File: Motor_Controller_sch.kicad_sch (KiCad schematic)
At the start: 34 parts, among them J10 1190304, J15 1190304, J17 Barrel_Jack, J2 GND, J3 RX, J4 TX, J5 RESET, J6 1098168, J9 1098168, U5 MCP23017_SP, U6 ATmega328-P, U7 L7805, U8 ULN2003

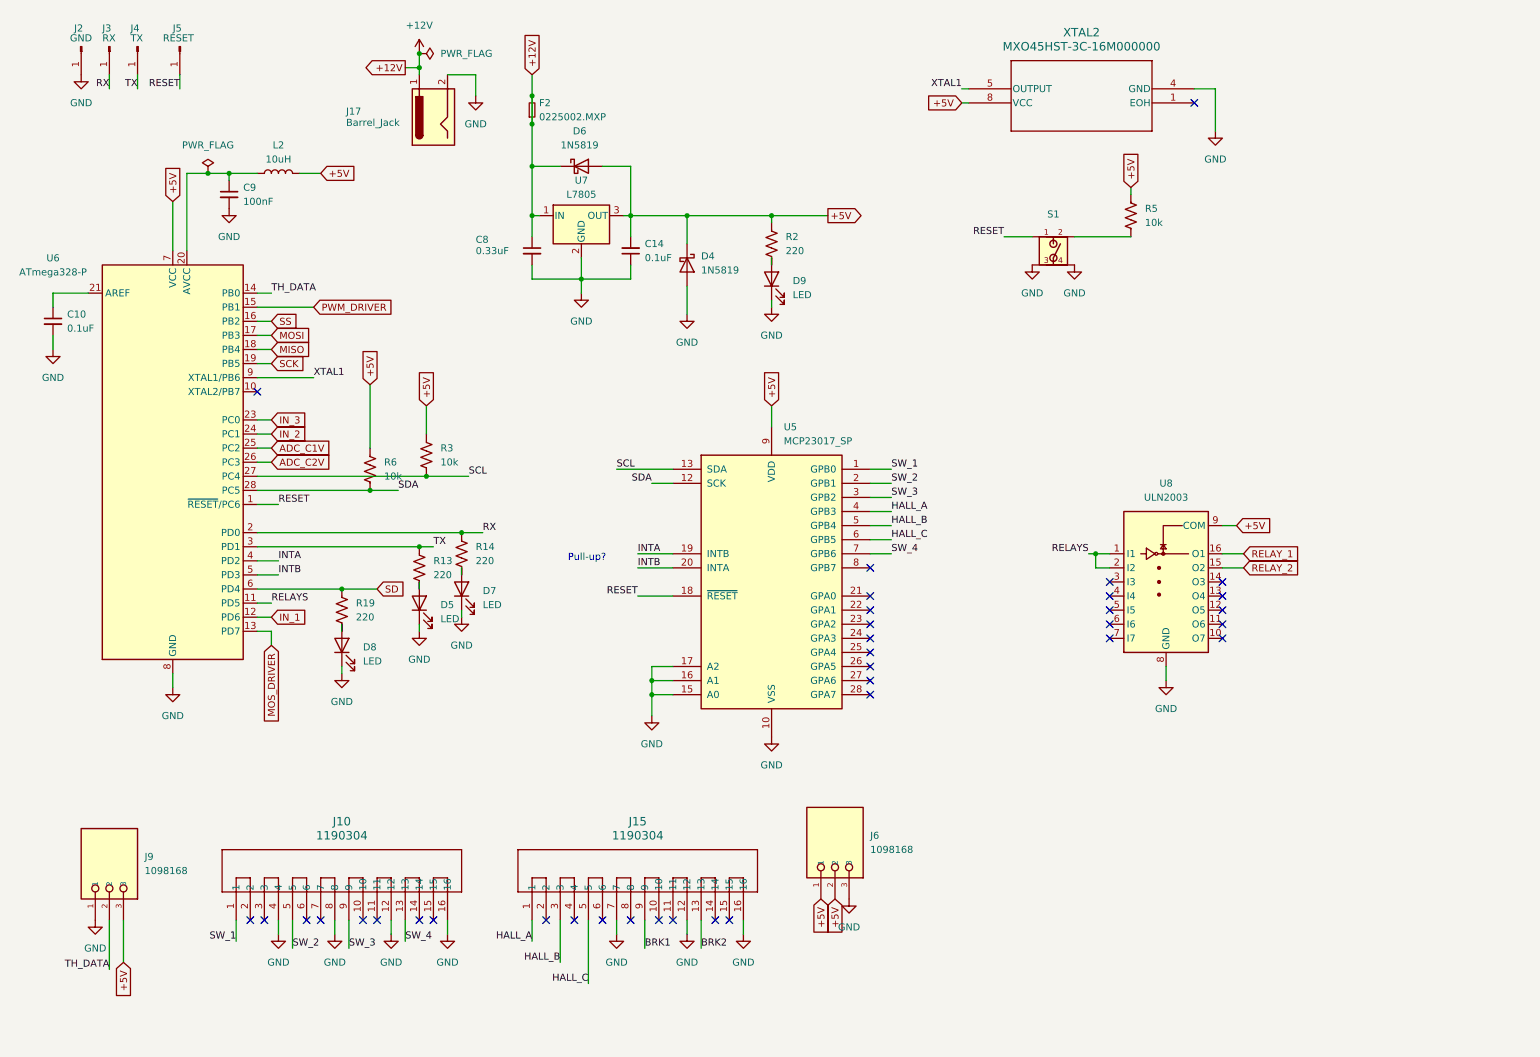
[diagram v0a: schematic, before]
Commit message: Made progress on the PCB, and adressed small issues regarding the schematic
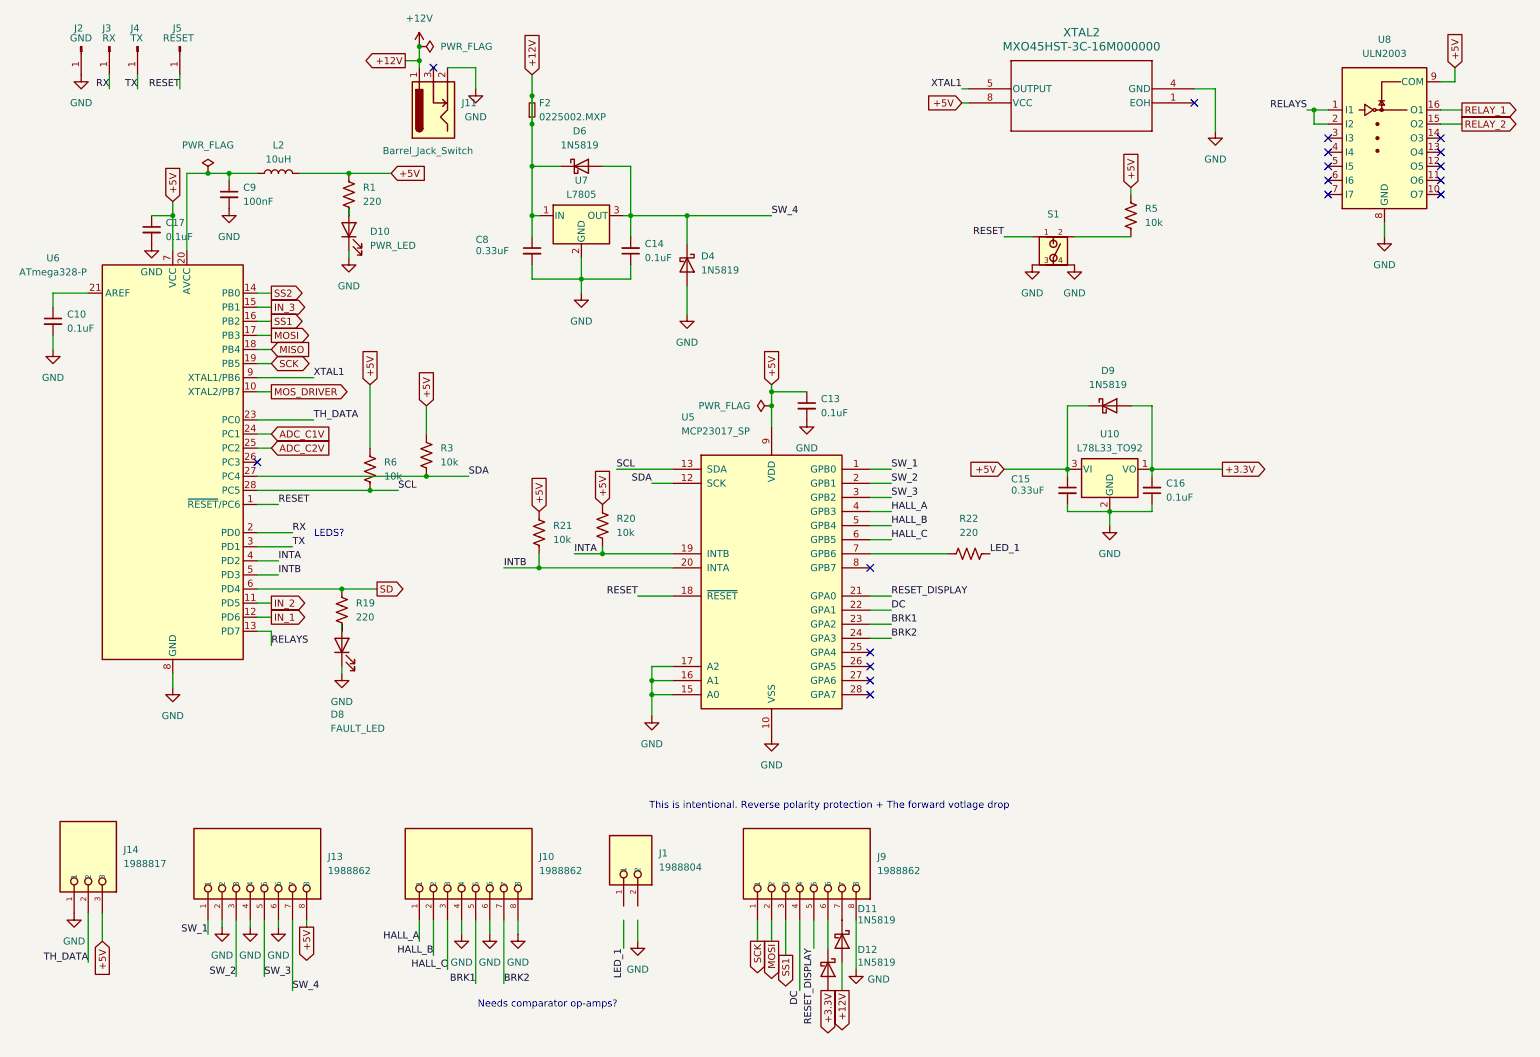
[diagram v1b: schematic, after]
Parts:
- removed D5, D7, D9: LED, symbol Device:LED
- removed J10, J15: 1190304, CONN16_1190304_PXC, symbol Terminal_1190304:1190304
- removed J17: Barrel_Jack, symbol Connector:Barrel_Jack
- removed J6, J9: 1098168, 1098168:PHOENIX_1098168, symbol Terminal_1098168:1098168
- removed R13, R14, R2: 220, symbol Device:R_US
- added C13, C16, C17: 0.1uF, Ceramic_Cap_5.08mm_Spacing:Ceramic_Cap_5.08mm_Spacing, symbol Device:C_Small
- added C15: 0.33uF, Ceramic_Cap_5.08mm_Spacing:Ceramic_Cap_5.08mm_Spacing, symbol Device:C_Small
- added D10: PWR_LED, LED_THT:LED_D5.0mm, symbol Device:LED
- added D11, D12, D9: 1N5819, Diode_THT:D_DO-41_SOD81_P10.16mm_Horizontal, symbol Diode:1N5819
- added J1: 1988804, Terminal_1988804:CONN_1988804, symbol 1988804:1988804
- added J10, J13, J9: 1988862, Terminal_1988862:PHOENIX_1988862, symbol 1988862:1988862
- added J11: Barrel_Jack_Switch, Barrel_Jack_PJ_002AH:PJ-002AH_CUD, symbol Connector:Barrel_Jack_Switch
- added J14: 1988817, Terminal_1988817:PHOENIX_1988817, symbol 1988817:1988817
- added R1, R22: 220, Resistor_THT:R_Axial_DIN0207_L6.3mm_D2.5mm_P10.16mm_Horizontal, symbol Device:R_US
- added R20, R21: 10k, Resistor_THT:R_Axial_DIN0207_L6.3mm_D2.5mm_P10.16mm_Horizontal, symbol Device:R_US
- added U10: L78L33_TO92, Package_TO_SOT_THT:TO-92_Inline, symbol Regulator_Linear:L78L33_TO92
- C10, C14, C8, C9: footprint (none) -> Ceramic_Cap_5.08mm_Spacing:Ceramic_Cap_5.08mm_Spacing
- D8: value LED -> FAULT_LED; footprint (none) -> LED_THT:LED_D5.0mm
- F2: footprint (none) -> Fuse_Holder_02540101Z:FUSE_254_PC_LTF
- J2, J3, J4, J5: footprint (none) -> Connector_PinHeader_1.00mm:PinHeader_1x01_P1.00mm_Vertical
- L2: footprint (none) -> Inductor_RLB0712_100KL:IND_BOURNS_RLB0712
- R19, R3, R5, R6: footprint (none) -> Resistor_THT:R_Axial_DIN0207_L6.3mm_D2.5mm_P10.16mm_Horizontal
- S1: footprint TS02-66-50-BK-160-LCR-D:SW_TS02-66-50-BK-160-LCR-D -> TS02_66_50_BK_160_LCR_D:SW_TS02-66-50-BK-160-LCR-D
- U5, U6: footprint Package_DIP:DIP-28_W7.62mm -> Package_DIP:DIP-28_W7.62mm_Socket
- U7: footprint (none) -> Package_TO_SOT_THT:TO-220-3_Vertical
- U8: footprint (none) -> Package_DIP:DIP-16_W7.62mm_Socket
- XTAL2: footprint (none) -> MXO45HST-3C-16M000000:MXO45HST-3C-16M000000
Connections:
- net PWM_DRIVER is gone; now on net IN_3: U6.15 (PB1)
- net +12V: now also D11.2 (A), J11.1
- net +5V: now also C13.1, C15.1, C17.1, D9.1 (K), J13.8, J14.3, R1.1, R20.1, R21.1, U10.3 (VI); no longer C14.2, D4.1 (K), D6.2 (A), U7.3 (OUT)
- net ADC_C1V: now also U6.24 (PC1); no longer U6.25 (PC2)
- net ADC_C2V: now also U6.25 (PC2); no longer U6.26 (PC3)
- net BRK1: now also U5.23 (GPA2), J10.5
- net BRK2: now also U5.24 (GPA3), J10.7
- net GND: now also C13.2, C15.2, C16.1, C17.2, D10.1 (K), J10.4, J10.6, J10.8, J11.2, J13.2, J13.4, J13.6, J14.1, J9.8, U10.2 (GND)
- net HALL_A: now also J10.1
- net HALL_B: now also J10.2
- net HALL_C: now also J10.3
- net INTA: now also R20.2
- net INTB: now also R21.2
- net IN_2: now also U6.11 (PD5); no longer U6.24 (PC1)
- net IN_3: no longer U6.23 (PC0)
- net MOSI: now also J9.2
- net MOS_DRIVER: now also U6.10 (XTAL2/PB7); no longer U6.13 (PD7)
- net RELAYS: now also U6.13 (PD7); no longer U6.11 (PD5)
- net SCK: now also J9.1
- net SCL: now also R6.2, U6.28 (PC5); no longer R3.2, U6.27 (PC4)
- net SDA: now also R3.2, U6.27 (PC4); no longer R6.2, U6.28 (PC5)
- net SW_1: now also J13.1
- net SW_2: now also J13.3
- net SW_3: now also J13.5
- net SW_4: now also C14.2, D4.1 (K), D6.2 (A), U7.3 (OUT), J13.7; no longer U5.7 (GPB6)
- net TH_DATA: now also U6.23 (PC0), J14.2; no longer U6.14 (PB0)
- net RESET_DISPLAY: now reaches U5.21 (GPA0)
- net RESET_DISPLAY: now also J9.5
- net DC: now reaches U5.22 (GPA1)
- net DC: now also J9.4
- net SS renamed SS1
- net SS1: now also J9.3
- new net: R22.2, U5.7 (GPB6)
- new net: D10.2 (A), R1.2
- new net: D11.1 (K), J9.7
- new net: D12.1 (K), J9.6
- new net +3.3V: C16.2, D12.2 (A), D9.2 (A), U10.1 (VO)
- new net LED_1: R22.1
- new net SS2: U6.14 (PB0)
- no-connect marks 37 -> 18
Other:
- note added: "LEDS?"
- note added: "Needs comparator op-amps?"
- note added: "This is intentional. Reverse polarity protection + The forward votlage drop"
- note removed: "Pull-up?"
- moved on the sheet: U8
